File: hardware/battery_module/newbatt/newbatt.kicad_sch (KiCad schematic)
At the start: 28 parts, among them J1 Barrel_Jack_MountingPin, J2 Conn_02x10_Odd_Even, U4 BQ24210DQCR

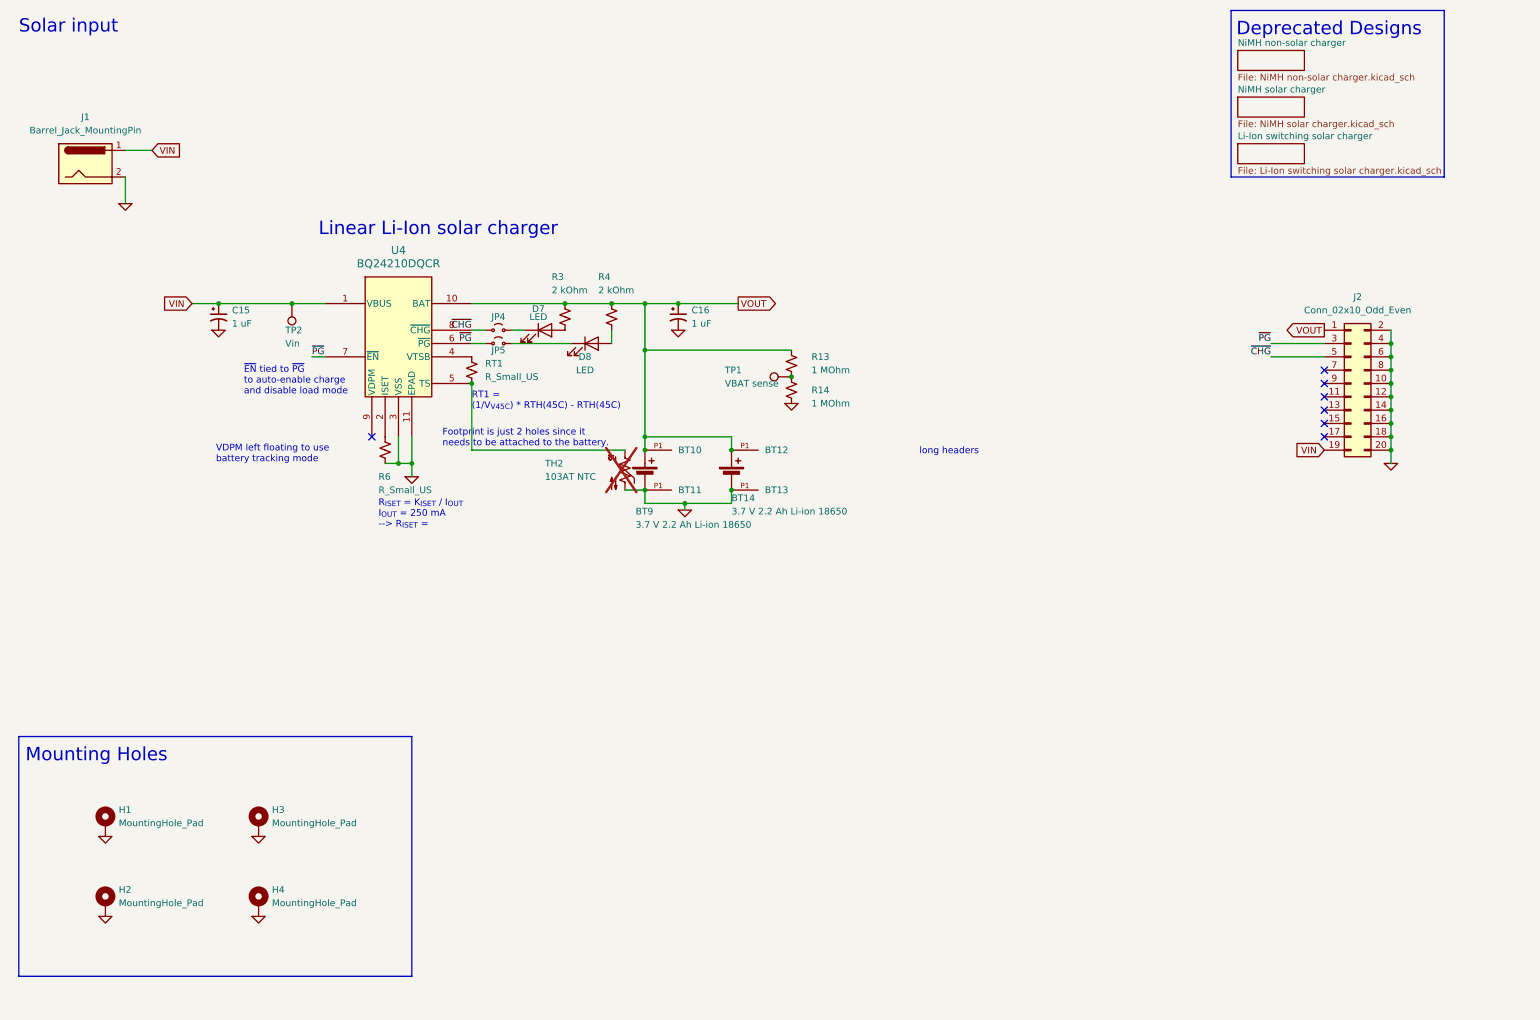
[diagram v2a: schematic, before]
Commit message: battery switch, fuse, and rerouted traces
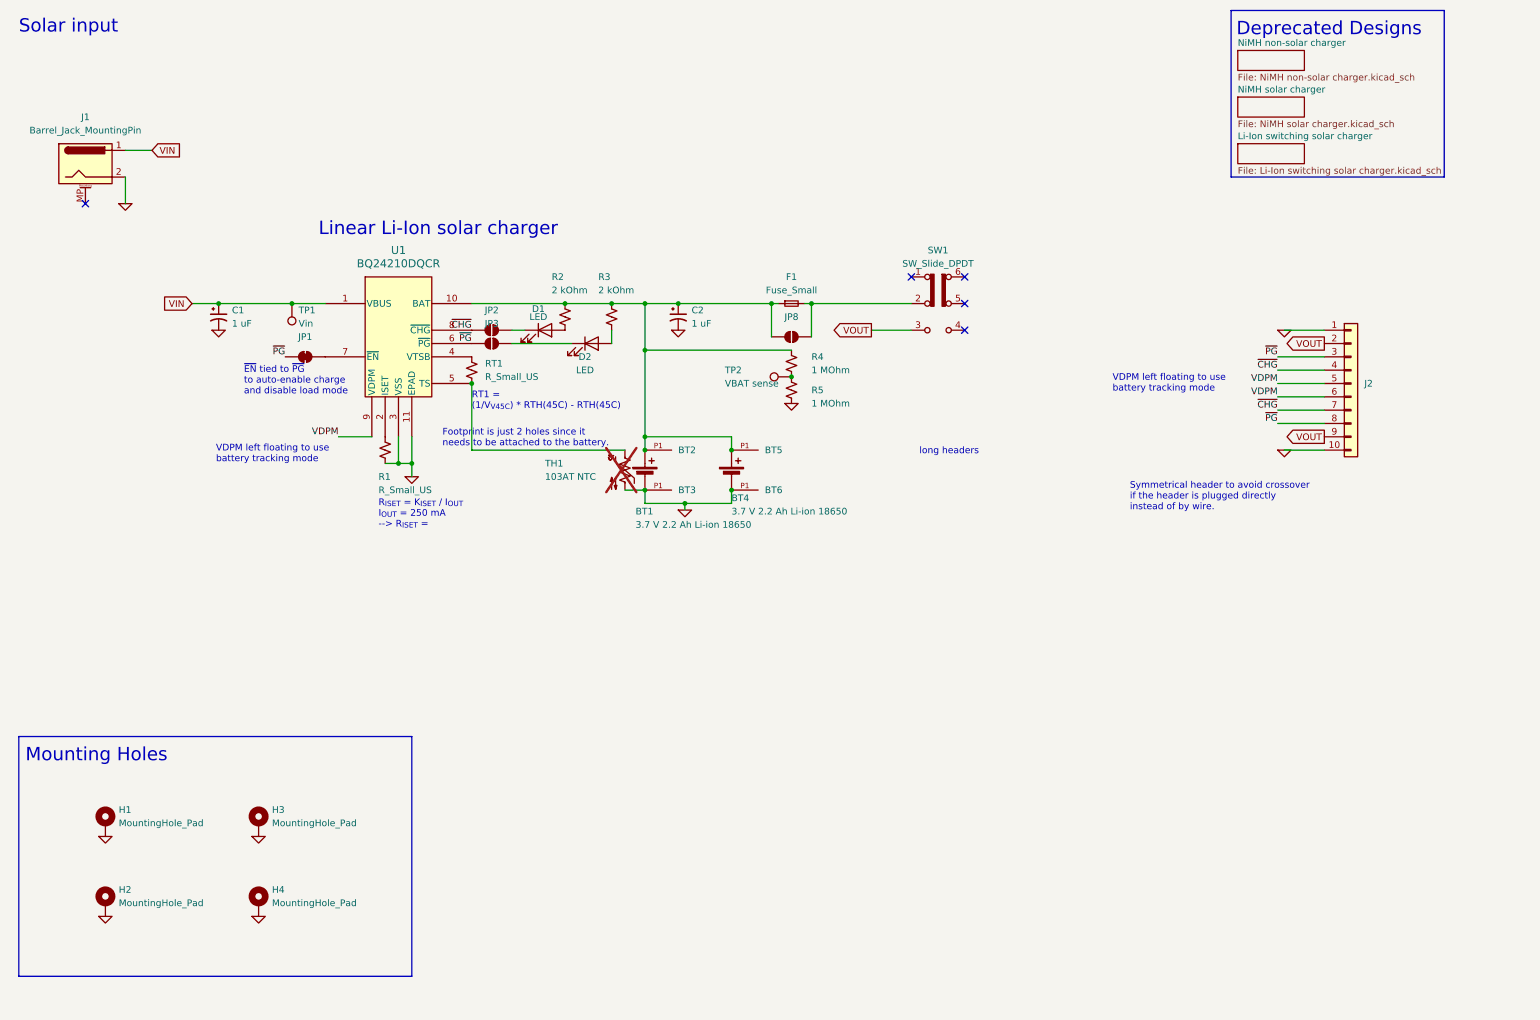
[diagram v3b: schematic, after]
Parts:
- removed JP4, JP5: Jumper_2_Small_Open, Jumper:SolderJumper-2_P1.3mm_Open_RoundedPad1.0x1.5mm, symbol Jumper:Jumper_2_Small_Open
- added F1: Fuse_Small, Fuse:Fuseholder_Clip-5x20mm_Keystone_3517_Inline_P23.11x6.76mm_D1.70mm_Horizontal, symbol Device:Fuse_Small
- added JP1: SolderJumper_2_Bridged, Jumper:SolderJumper-2_P1.3mm_Bridged_RoundedPad1.0x1.5mm, symbol Jumper:SolderJumper_2_Bridged
- added JP2, JP3, JP8: SolderJumper_2_Open, Jumper:SolderJumper-2_P1.3mm_Open_RoundedPad1.0x1.5mm, symbol Jumper:SolderJumper_2_Open
- added SW1: SW_Slide_DPDT, JS202011SCQN:JS202011SCQN, symbol Switch:SW_Slide_DPDT
- J1: symbol Connector:Barrel_Jack -> Connector:Barrel_Jack_MountingPin
- J2: value Conn_02x10_Odd_Even -> Conn_01x10; footprint Connector_PinHeader_2.54mm:PinHeader_2x10_P2.54mm_Vertical -> Connector_PinSocket_2.54mm:PinSocket_1x10_P2.54mm_Horizontal; symbol Connector_Generic:Conn_02x10_Odd_Even -> Connector_Generic:Conn_01x10
- renumbered BT9 to BT1, BT10 to BT2, BT11 to BT3, BT14 to BT4, BT12 to BT5, BT13 to BT6, C15 to C1, C16 to C2, D7 to D1, D8 to D2, R6 to R1, R3 to R2, R4 to R3, R13 to R4, R14 to R5, TH2 to TH1, TP2 to TP1, TP1 to TP2, U4 to U1
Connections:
- net 0: now also J2.1 (Pin_1); no longer J2.12 (Pin_12), J2.14 (Pin_14), J2.16 (Pin_16), J2.18 (Pin_18), J2.2 (Pin_2), J2.20 (Pin_20), J2.4 (Pin_4), J2.6 (Pin_6), J2.8 (Pin_8)
- net VIN: no longer J2.19 (Pin_19)
- net VOUT: now also J2.2 (Pin_2), J2.9 (Pin_9), SW1.3 (C); no longer BT1.1 (+), BT2.P1, BT4.1 (+), BT5.P1, C2.1, J2.1 (Pin_1), R2.1, R3.1, R4.1, U1.10 (BAT)
- net ~{CHG}: now also J2.4 (Pin_4), J2.7 (Pin_7), JP2.1 (A); no longer J2.5 (Pin_5)
- net ~{PG}: now also J2.8 (Pin_8), JP1.1 (A), JP3.1 (A); no longer U1.7 (~{EN})
- net at D1.1 (K): now also JP2.2 (B)
- net at D2.1 (K): now also JP3.2 (B)
- net VDPM: now reaches U1.9 (VDPM)
- net VDPM: now also J2.5 (Pin_5), J2.6 (Pin_6)
- new net: BT1.1 (+), BT2.P1, BT4.1 (+), BT5.P1, C2.1, F1.1, JP8.1 (A), R2.1, R3.1, R4.1, U1.10 (BAT)
- new net: JP1.2 (B), U1.7 (~{EN})
- new net: F1.2, JP8.2 (B), SW1.2 (B)
- no-connect marks 7 -> 5
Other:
- note added: "Symmetrical header to avoid crossover if the header is plugged directly instead of by wire."

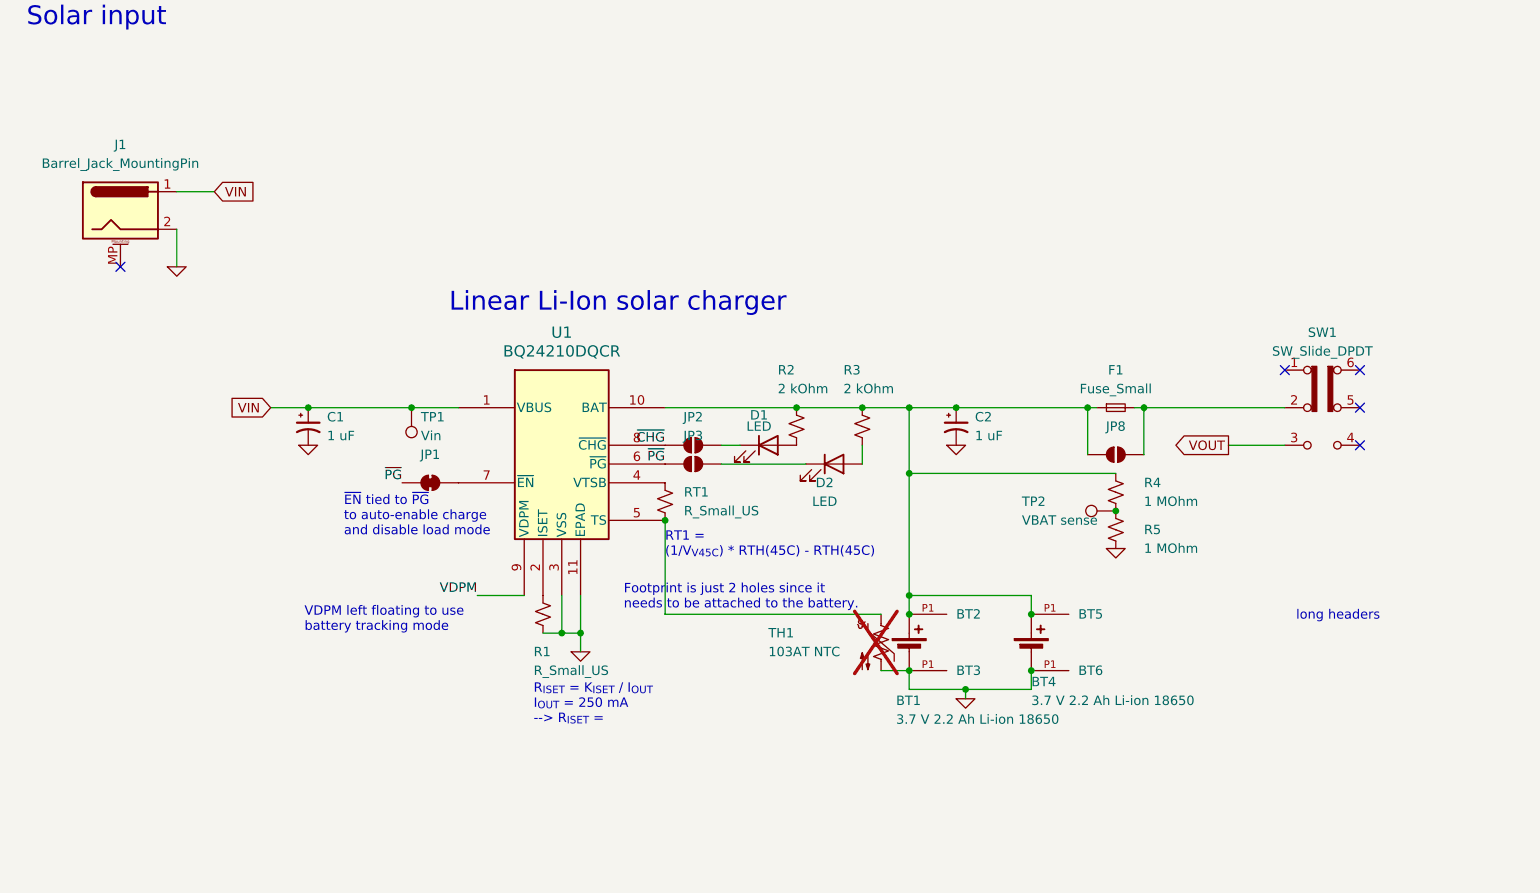
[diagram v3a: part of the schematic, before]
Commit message: glass fuse and updated footprints
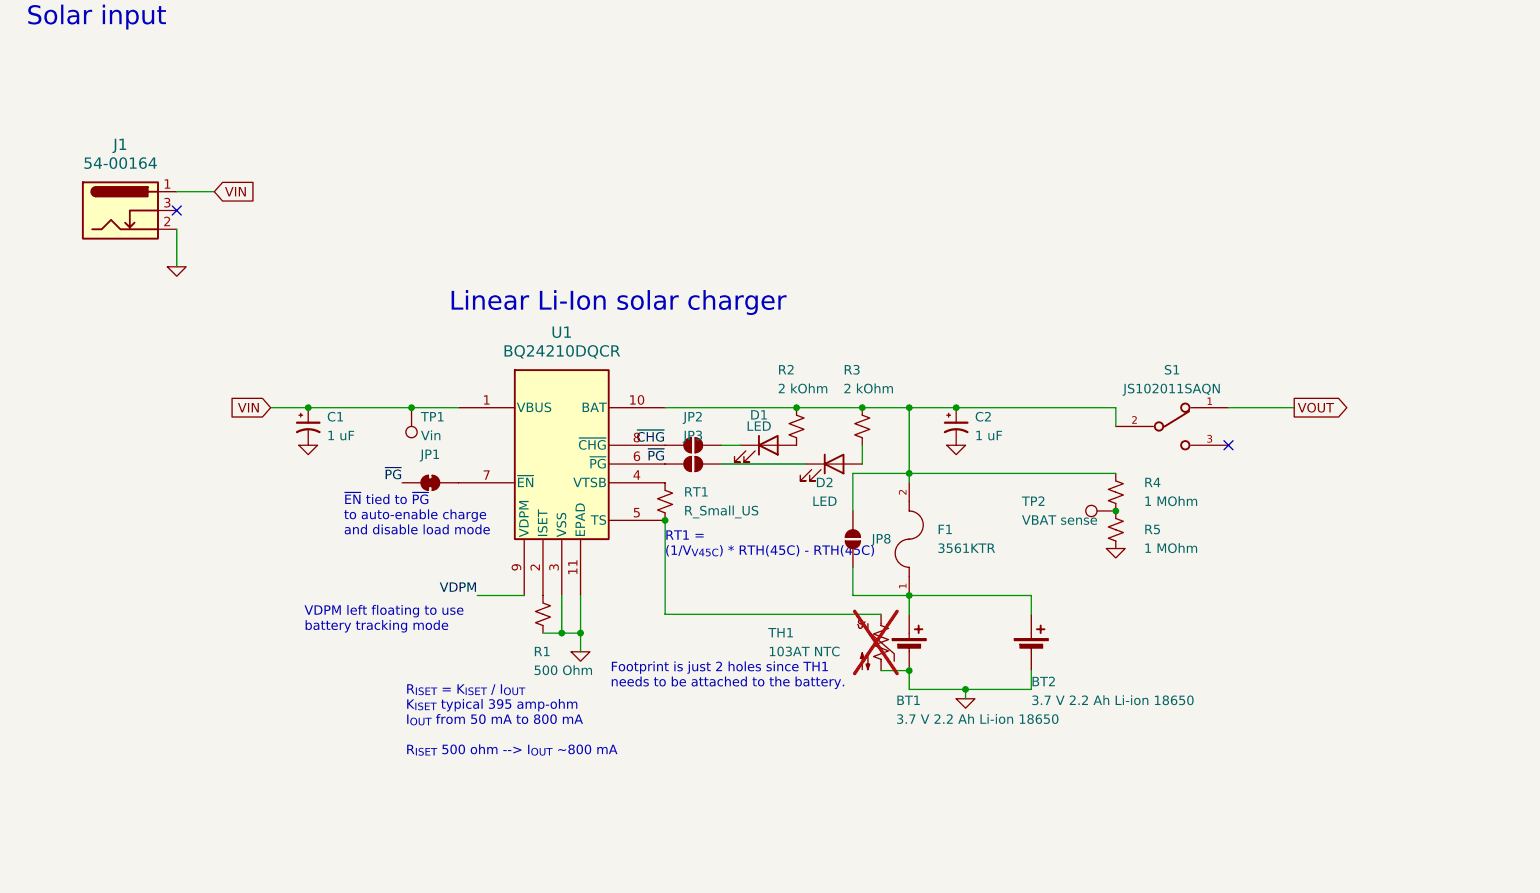
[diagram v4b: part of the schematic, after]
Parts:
- removed BT2, BT3, BT5, BT6: 254TR, Keystone254TR:BAT_254TR, symbol Keystone254TR:254TR
- removed F1: Fuse_Small, Fuse:Fuseholder_Clip-5x20mm_Keystone_3517_Inline_P23.11x6.76mm_D1.70mm_Horizontal, symbol Device:Fuse_Small
- removed J1: Barrel_Jack_MountingPin, Connector_BarrelJack:BarrelJack_Horizontal, symbol Connector:Barrel_Jack_MountingPin
- removed SW1: SW_Slide_DPDT, JS202011SCQN:JS202011SCQN, symbol Switch:SW_Slide_DPDT
- added F1: 3561KTR, 3561KTR:FUSE_3561KTR, symbol 3561KTR:3561KTR
- added J1: 54-00164, 54-00164:TENSILITY_54-00164, symbol 54-00164:54-00164
- added S1: JS102011SAQN, JS102011SAQN:SW_JS102011SAQN, symbol JS102011SAQN:JS102011SAQN
- BT1: footprint Connector_JST:JST_PH_S2B-PH-K_1x02_P2.00mm_Horizontal -> Keystone254TR:BAT_254TR
- BT2: renamed from BT4; footprint Connector_JST:JST_PH_S2B-PH-K_1x02_P2.00mm_Horizontal -> Keystone254TR:BAT_254TR
- R1: value R_Small_US -> 500 Ohm
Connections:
- net 0: now also J1.2
- net VIN: now also J1.1
- net VOUT: now also S1.1
- net at C2.1, R2.1, R3.1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: now also JP8.2 (B), F1.2, S1.2; no longer BT1.1 (+), BT2.1 (+), JP8.1 (A)
- new net: BT1.1 (+), BT2.1 (+), F1.1, JP8.1 (A)
- no-connect marks 5 -> 2
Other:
- note added: "Footprint is just 2 holes since TH1 needs to be attached to the battery."
- note added: "R_{ISET} = K_{ISET} / I_{OUT} K_{ISET} typical 395 amp-ohm I_{OUT} from 50 mA to 800 mA R_{ISET} 500 ohm --> I_{OUT} ~800 mA"
- note removed: "Footprint is just 2 holes since it needs to be attached to the battery."
- note removed: "R_{ISET} = K_{ISET} / I_{OUT} I_{OUT} = 250 mA --> R_{ISET} ="
- note removed: "long headers"
- moved on the sheet: JP8
